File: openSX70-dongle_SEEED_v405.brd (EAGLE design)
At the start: 29.3 x 24.7 mm, 24 parts, among them SW1 MK-12C02 G1.5, SW2 MK-12C02 G1.5, X1 1503_02

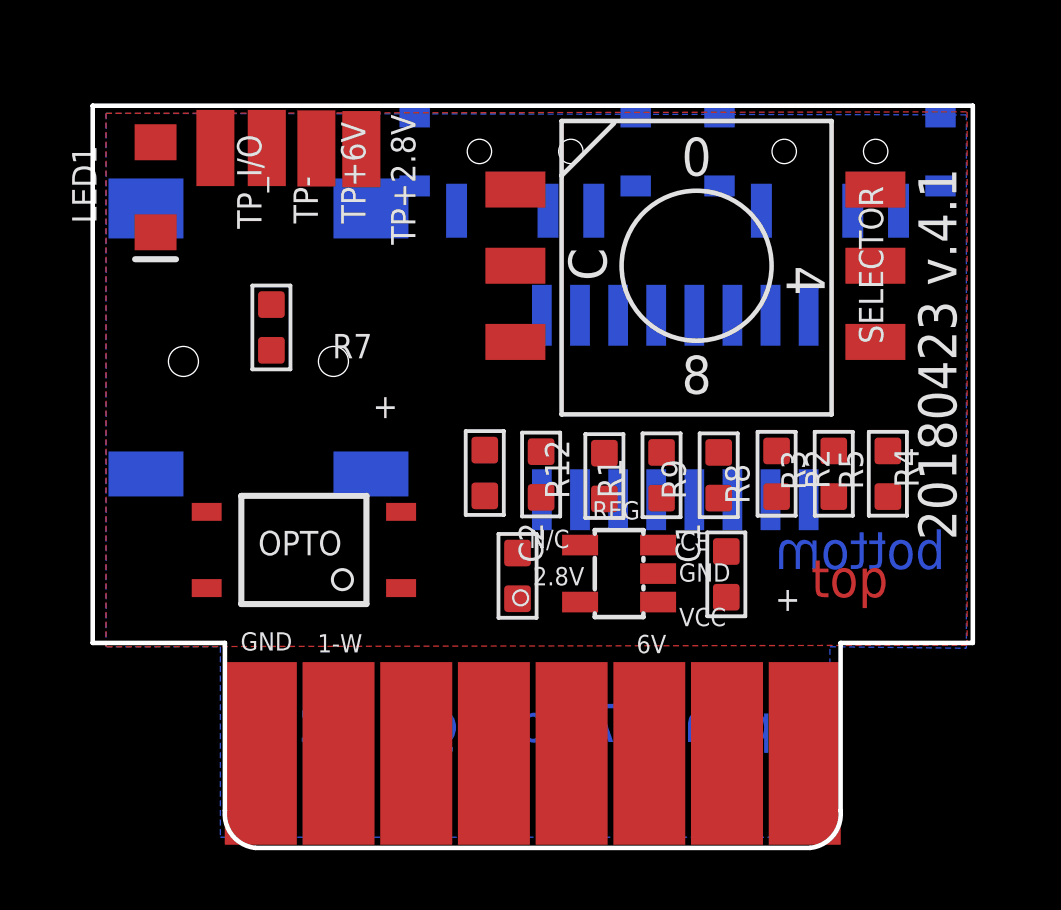
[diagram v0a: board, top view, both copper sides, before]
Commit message: Working towards a all SMD smaller uDongle2
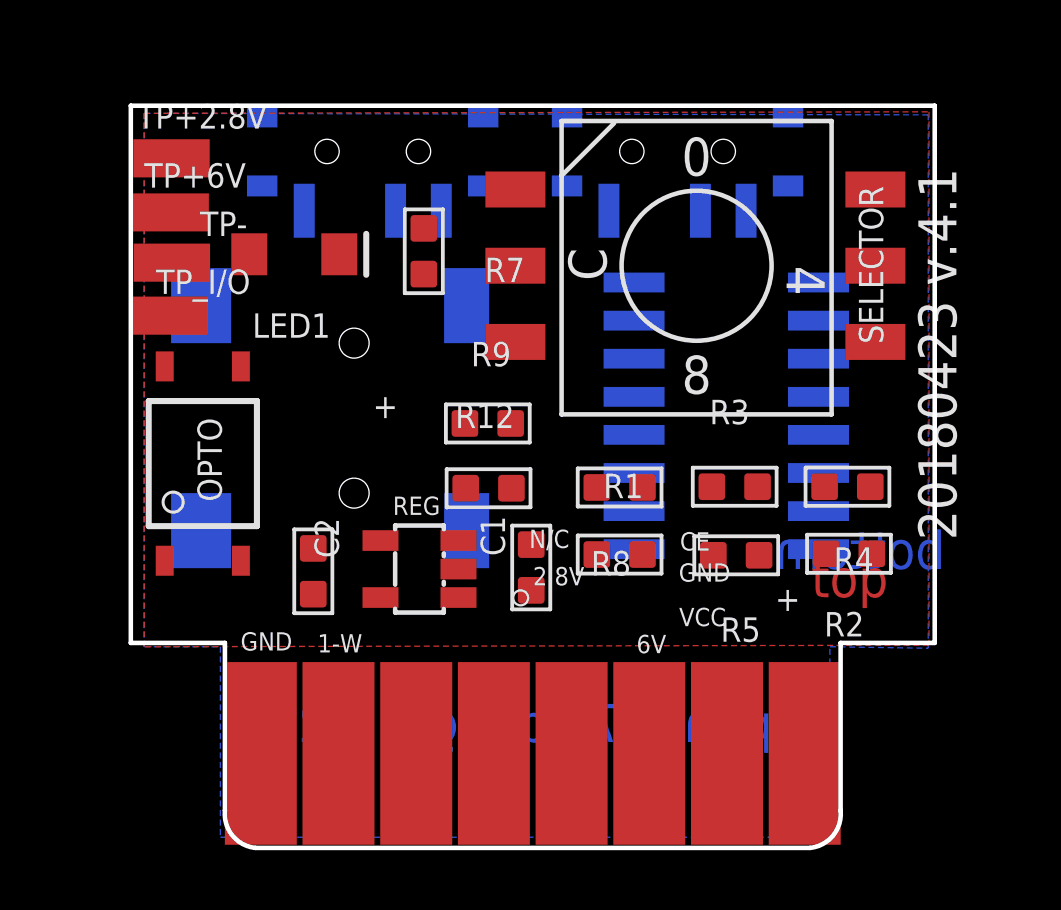
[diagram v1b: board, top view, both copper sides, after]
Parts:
- moved X1 9.67 mm to (12.7, 15.2), turned to 270 degrees
- moved C2 6.81 mm to (18.3, 10.1)
- moved REG 6.66 mm to (21.9, 10.2)
- moved C1 6.51 mm to (25.6, 10.3)
- moved TP+2.8V 6.33 mm to (13.6, 23.9), turned to 90 degrees
- moved TP_I/O 5.79 mm to (13.6, 18.7), turned to 90 degrees
- moved R7 5.68 mm to (22.0, 20.8)
- moved OPTO 5.33 mm to (14.0, 13.7), turned to 90 degrees
- moved TP+6V 5.30 mm to (13.6, 22.1), turned to 90 degrees
- moved LED1 5.13 mm to (17.7, 20.7), turned to 0 degrees
- moved SW2 5.08 mm to (30.5, 24.1)
- moved SW1 5.08 mm to (20.3, 24.1)
- moved TP- 4.96 mm to (13.6, 20.4), turned to 90 degrees
- moved R9 4.26 mm to (24.2, 15.1), turned to 270 degrees
- moved R1 3.74 mm to (28.5, 10.7), turned to 270 degrees
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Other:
- board size 29.3 x 24.7 mm -> 26.8 x 24.7 mm
